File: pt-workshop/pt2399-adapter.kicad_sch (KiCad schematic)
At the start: 24 parts, among them U201 L78L05, U202 PT2399-Detailed

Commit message: 10 pin socket
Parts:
- added C216: 4.7u, Capacitor_SMD:CP_Elec_4x5.4, symbol Device:C_Polarized_Small
- added R208: 10K, Resistor_SMD:R_0603_1608Metric_Pad0.98x0.95mm_HandSolder, symbol Device:R_Small
- C201, C215: footprint Capacitor_SMD:CP_Elec_5x5.4 -> Capacitor_Tantalum_SMD:CP_EIA-3216-10_Kemet-I_Pad1.58x1.35mm_HandSolder; LCSC C380314 -> (none); Mouser 710-865080440002 -> (none)
- C203: renamed from C202; footprint Capacitor_SMD:CP_Elec_4x5.4 -> Capacitor_Tantalum_SMD:CP_EIA-3216-10_Kemet-I_Pad1.58x1.35mm_HandSolder; LCSC C264238 -> (none); Mouser 710-865080440002 -> (none)
- C205: renamed from C204; footprint Capacitor_SMD:CP_Elec_4x5.4 -> Capacitor_Tantalum_SMD:CP_EIA-3216-10_Kemet-I_Pad1.58x1.35mm_HandSolder; LCSC C380314 -> (none); Mouser 710-865080440002 -> (none)
- U202: footprint Package_DIP:DIP-16_W7.62mm -> Package_SO:SOIC-16_3.9x9.9mm_P1.27mm
- renumbered C203 to C202, C205 to C204
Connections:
- net GND: now also R208.2
- net Out: now also C216.2, R208.1; no longer C213.2, R207.1
- new net: C213.2, C216.1, R207.1
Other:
- moved on the sheet: C202, C204, C206, C207, C208, C209, C210, C211, C212, C213, C214, C215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

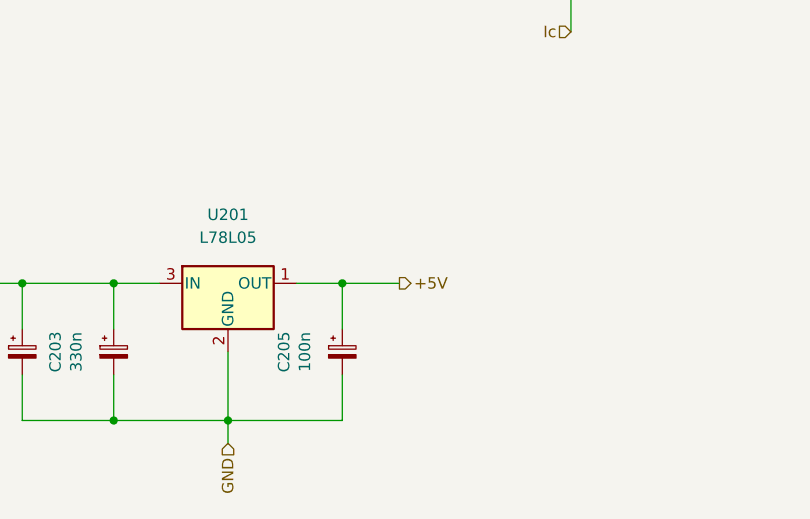
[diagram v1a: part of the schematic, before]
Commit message: Mapped components
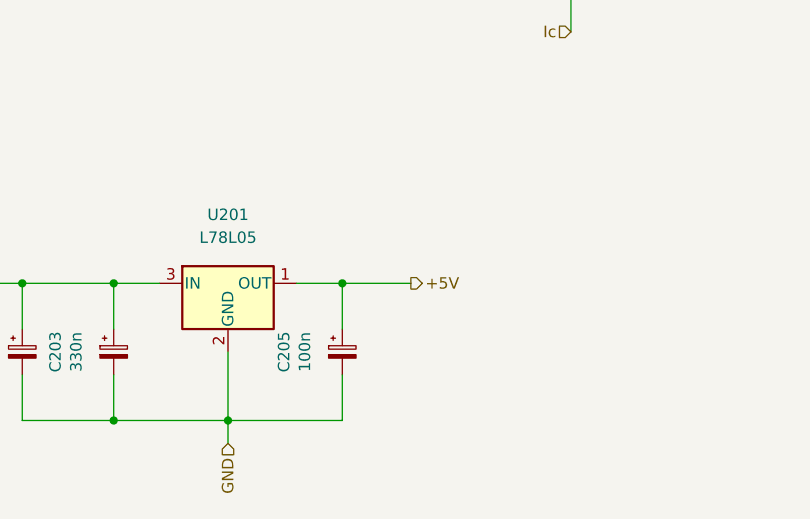
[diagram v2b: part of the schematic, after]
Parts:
- C201, C215: LCSC (none) -> C128254
- C202, C216: LCSC C213488 -> C72511
- C203: LCSC (none) -> C212667
- C205: LCSC (none) -> C1952859
- C206, C212: LCSC C107054 -> C694498
- C208, C209: LCSC C519438 -> C57112
- C210: LCSC C190576 -> C415537
- C213: LCSC C57112 -> C91367
- C214: LCSC C497032 -> C57112
- R201, R206: LCSC C100780 -> C22809
- R202, R203, R204, R205: LCSC C98220 -> C25804
- R207: LCSC C365194 -> C23189
- R208: LCSC (none) -> C25804
- U202: LCSC (none) -> C126407
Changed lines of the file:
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@@
-    (stroke (width 0) (type default) (color 0 0 0 0))
-  )
-  (wire (pts (xy 63.5 160.02) (xy 69.85 160.02))
     (stroke (width 0) (type default) (color 0 0 0 0))
   )
@@
   )
   (wire (pts (xy 180.34 83.82) (xy 180.34 91.44))
+    (stroke (width 0) (type default) (color 0 0 0 0))
+  )
+  (wire (pts (xy 63.5 160.02) (xy 71.12 160.02))
     (stroke (width 0) (type default) (color 0 0 0 0))
   )
@@
     (effects (font (size 1.27 1.27)) (justify left))
   )
-  (hierarchical_label "+5V" (shape output) (at 69.85 160.02 0)
+  (hierarchical_label "+5V" (shape output) (at 71.12 160.02 0)
     (effects (font (size 1.27 1.27)) (justify left))
   )
@@
       (effects (font (size 1.27 1.27)) hide)
     )
-    (property "LCSC" "C365194" (id 4) (at 182.88 27.94 0)
+    (property "LCSC" "C23189" (id 4) (at 182.88 27.94 0)
       (effects (font (size 1.27 1.27)) hide)
     )
@@
       (effects (font (size 1.27 1.27)) hide)
     )
-    (property "LCSC" "C107054" (id 4) (at 81.28 53.34 0)
+    (property "LCSC" "C694498" (id 4) (at 81.28 53.34 0)
       (effects (font (size 1.27 1.27)) hide)
     )
@@
       (effects (font (size 1.27 1.27)) hide)
     )
-    (property "LCSC" "C519438" (id 4) (at 134.62 132.08 0)
+    (property "LCSC" "C57112" (id 4) (at 134.62 132.08 0)
       (effects (font (size 1.27 1.27)) hide)
     )
@@
       (effects (font (size 1.27 1.27)) hide)
     )
-    (property "LCSC" "C213488" (id 4) (at 200.66 27.94 0)
+    (property "LCSC" "C72511" (id 4) (at 200.66 27.94 0)
       (effects (font (size 1.27 1.27)) hide)
     )
@@
       (effects (font (size 1.27 1.27)) hide)
     )
-    (property "LCSC" "" (id 4) (at 63.5 167.64 0)
+    (property "LCSC" "C1952859" (id 4) (at 63.5 167.64 0)
       (effects (font (size 1.27 1.27)) hide)
     )
@@
       (effects (font (size 1.27 1.27)) hide)
     )
-    (property "LCSC" "C57112" (id 4) (at 187.96 33.02 0)
+    (property "LCSC" "C91367" (id 4) (at 187.96 33.02 0)
       (effects (font (size 1.27 1.27)) hide)
     )
@@
       (effects (font (size 1.27 1.27)) hide)
     )
-    (property "LCSC" "C98220" (id 4) (at 154.94 27.94 0)
+    (property "LCSC" "C25804" (id 4) (at 154.94 27.94 0)
       (effects (font (size 1.27 1.27)) hide)
     )
@@
       (effects (font (size 1.27 1.27)) hide)
     )
-    (property "LCSC" "C100780" (id 4) (at 43.18 53.34 0)
+    (property "LCSC" "C22809" (id 4) (at 43.18 53.34 0)
       (effects (font (size 1.27 1.27)) hide)
     )
@@
       (effects (font (size 1.27 1.27)) hide)
     )
-    (property "LCSC" "C519438" (id 4) (at 139.7 129.54 0)
+    (property "LCSC" "C57112" (id 4) (at 139.7 129.54 0)
       (effects (font (size 1.27 1.27)) hide)
     )
@@
       (effects (font (size 1.27 1.27)) hide)
     )
-    (property "LCSC" "" (id 4) (at 187.96 93.98 0)
+    (property "LCSC" "C128254" (id 4) (at 187.96 93.98 0)
       (effects (font (size 1.27 1.27)) hide)
     )
@@
       (effects (font (size 1.27 1.27)) hide)
     )
-    (property "LCSC" "C100780" (id 4) (at 162.56 19.05 0)
+    (property "LCSC" "C22809" (id 4) (at 162.56 19.05 0)
       (effects (font (size 1.27 1.27)) hide)
     )
@@
       (effects (font (size 1.27 1.27)) hide)
     )
-    (property "LCSC" "C213488" (id 4) (at 30.48 53.34 0)
+    (property "LCSC" "C72511" (id 4) (at 30.48 53.34 0)
       (effects (font (size 1.27 1.27)) hide)
     )
@@
       (effects (font (size 1.27 1.27)) hide)
     )
-    (property "LCSC" "C190576" (id 4) (at 149.86 33.02 0)
+    (property "LCSC" "C415537" (id 4) (at 149.86 33.02 0)
       (effects (font (size 1.27 1.27)) hide)
     )
@@
       (effects (font (size 1.27 1.27)) hide)
     )
-    (property "LCSC" "C497032" (id 4) (at 187.96 83.82 0)
+    (property "LCSC" "C57112" (id 4) (at 187.96 83.82 0)
       (effects (font (size 1.27 1.27)) hide)
     )
@@
       (effects (font (size 1.27 1.27)) hide)
     )
-    (property "LCSC" "" (id 4) (at 27.94 167.64 0)
+    (property "LCSC" "C128254" (id 4) (at 27.94 167.64 0)
       (effects (font (size 1.27 1.27)) hide)
     )
@@
       (effects (font (size 1.27 1.27)) hide)
     )
-    (property "LCSC" "C98220" (id 4) (at 142.24 27.94 0)
+    (property "LCSC" "C25804" (id 4) (at 142.24 27.94 0)
       (effects (font (size 1.27 1.27)) hide)
     )
@@
     )
     (property "Datasheet" "https://www.electrosmash.com/pt2399-analysis" (id 3) (at 181.61 92.075 0)
+      (effects (font (size 1.27 1.27)) hide)
+    )
+    (property "LCSC" "C126407" (id 4) (at 124.46 88.9 0)
       (effects (font (size 1.27 1.27)) hide)
     )
@@
       (effects (font (size 1.27 1.27)) hide)
     )
-    (property "LCSC" "C107054" (id 4) (at 167.64 27.94 0)
+    (property "LCSC" "C694498" (id 4) (at 167.64 27.94 0)
       (effects (font (size 1.27 1.27)) hide)
     )
@@
       (effects (font (size 1.27 1.27)) hide)
     )
-    (property "LCSC" "" (id 4) (at 38.1 167.64 0)
+    (property "LCSC" "C212667" (id 4) (at 38.1 167.64 0)
       (effects (font (size 1.27 1.27)) hide)
     )
@@
       (effects (font (size 1.27 1.27)) hide)
     )
-    (property "LCSC" "C98220" (id 4) (at 66.04 53.34 0)
+    (property "LCSC" "C25804" (id 4) (at 66.04 53.34 0)
       (effects (font (size 1.27 1.27)) hide)
     )
@@
       (effects (font (size 1.27 1.27)) hide)
     )
-    (property "LCSC" "C98220" (id 4) (at 66.04 40.64 0)
+    (property "LCSC" "C25804" (id 4) (at 66.04 40.64 0)
       (effects (font (size 1.27 1.27)) hide)
     )
@@
       (effects (font (size 1.27 1.27)) hide)
     )
+    (property "LCSC" "C25804" (id 4) (at 214.63 33.02 0)
+      (effects (font (size 1.27 1.27)) hide)
+    )

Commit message: wip
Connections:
- net In: now also C202.2; no longer C202.1
- net at R201.1: now also C202.1; no longer C202.2
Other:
- moved on the sheet: C202
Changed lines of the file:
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@@
     (pin "2")
   )
-  (symbol (lib_id "Device:C_Polarized_Small") (at 30.48 53.34 90) (unit 1)
+  (symbol (lib_id "Device:C_Polarized_Small") (at 30.48 53.34 270) (mirror x) (unit 1)
     (in_bom yes) (on_board yes)
     (property "Reference" "C202" (id 0) (at 30.48 48.26 90))

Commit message: jlc
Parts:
- C208, C209, C214: LCSC C57112 -> C497032
- C213: LCSC C91367 -> C3836718
- R202, R203, R204, R205: Mouser 603-RT0603DRE1010KL -> (none)
- U201: LCSC C347258 -> C42738
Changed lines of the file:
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@@
       (effects (font (size 1.27 1.27)) hide)
     )
-    (property "LCSC" "C57112" (id 4) (at 134.62 132.08 0)
+    (property "LCSC" "C497032" (id 4) (at 134.62 132.08 0)
       (effects (font (size 1.27 1.27)) hide)
     )
@@
       (effects (font (size 1.27 1.27)) hide)
     )
-    (property "LCSC" "C91367" (id 4) (at 187.96 33.02 0)
+    (property "LCSC" "C3836718" (id 4) (at 187.96 33.02 0)
       (effects (font (size 1.27 1.27)) hide)
     )
@@
       (effects (font (size 1.27 1.27)) hide)
     )
-    (property "Mouser" "603-RT0603DRE1010KL" (id 5) (at 154.94 27.94 0)
+    (property "Mouser" "" (id 5) (at 154.94 27.94 0)
       (effects (font (size 1.27 1.27)) hide)
     )
@@
       (effects (font (size 1.27 1.27)) hide)
     )
-    (property "LCSC" "C57112" (id 4) (at 139.7 129.54 0)
+    (property "LCSC" "C497032" (id 4) (at 139.7 129.54 0)
       (effects (font (size 1.27 1.27)) hide)
     )
@@
       (effects (font (size 1.27 1.27)) hide)
     )
-    (property "LCSC" "C57112" (id 4) (at 187.96 83.82 0)
+    (property "LCSC" "C497032" (id 4) (at 187.96 83.82 0)
       (effects (font (size 1.27 1.27)) hide)
     )
@@
       (effects (font (size 1.27 1.27)) hide)
     )
-    (property "Mouser" "603-RT0603DRE1010KL" (id 5) (at 142.24 27.94 0)
+    (property "Mouser" "" (id 5) (at 142.24 27.94 0)
       (effects (font (size 1.27 1.27)) hide)
     )
@@
       (effects (font (size 1.27 1.27)) hide)
     )
-    (property "Mouser" "603-RT0603DRE1010KL" (id 5) (at 66.04 53.34 0)
+    (property "Mouser" "" (id 5) (at 66.04 53.34 0)
       (effects (font (size 1.27 1.27)) hide)
     )
@@
       (effects (font (size 1.27 1.27)) hide)
     )
-    (property "Mouser" "603-RT0603DRE1010KL" (id 5) (at 66.04 40.64 0)
+    (property "Mouser" "" (id 5) (at 66.04 40.64 0)
       (effects (font (size 1.27 1.27)) hide)
     )
@@
       (effects (font (size 1.27 1.27)) hide)
     )
-    (property "LCSC" "C347258" (id 4) (at 50.8 160.02 0)
-      (effects (font (size 1.27 1.27)) hide)
-    )
+    (property "LCSC" "C42738" (id 4) (at 50.8 160.02 0)
+      (effects (font (size 1.27 1.27)) hide)
+    )

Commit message: PTT schem export
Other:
- company: (none) -> Pedal Markt
- title: (none) -> PTT
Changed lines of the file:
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@@
 (kicad_sch (version 20211123) (generator eeschema)
   (paper "A4")
+  (title_block
+    (title "PTT")
+    (date "2024-05-11")
+    (rev "v1rev2")
+    (company "Pedal Markt")
+    (comment 1 "Andrey Salomatin")
+  )
   (junction (at 187.96 27.94) (diameter 0) (color 0 0 0 0)
   )

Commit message: wip
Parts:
- C201, C215: LCSC C128254 -> C128253
- C202, C216: LCSC C72511 -> C5246584
- C208, C209, C214: value 100n -> 1u; LCSC C497032 -> C15849; Mouser 80-C0603C104M5RAUTO -> (none)
- R207: value 5.6K -> 1k; LCSC C23189 -> C21190; Mouser 603-RT0603DRD075K6L -> (none)
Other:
- note added: "dnp"
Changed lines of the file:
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@@
     (title "PTT")
     (date "2024-05-11")
-    (rev "v1rev2")
+    (rev "v1rev3")
     (company "Pedal Markt")
     (comment 1 "Andrey Salomatin")
@@
     (stroke (width 0) (type default) (color 0 0 0 0))
   )
+  (text "dnp" (at 190.5 38.1 0)
+    (effects (font (size 1.27 1.27)) (justify left bottom))
+  )
   (label "DEMOD_OUT" (at 154.94 50.8 90)
     (effects (font (size 1 1)) (justify left bottom))
@@
     (in_bom yes) (on_board yes)
     (property "Reference" "R207" (id 0) (at 182.88 23.495 90))
-    (property "Value" "5.6K" (id 1) (at 182.88 25.4 90))
+    (property "Value" "1k" (id 1) (at 182.88 25.4 90))
     (property "Footprint" "Resistor_SMD:R_0603_1608Metric_Pad0.98x0.95mm_HandSolder" (id 2) (at 182.88 27.94 0)
       (effects (font (size 1.27 1.27)) hide)
@@
       (effects (font (size 1.27 1.27)) hide)
     )
-    (property "LCSC" "C23189" (id 4) (at 182.88 27.94 0)
-      (effects (font (size 1.27 1.27)) hide)
-    )
-    (property "Mouser" "603-RT0603DRD075K6L" (id 5) (at 182.88 27.94 0)
+    (property "LCSC" "C21190" (id 4) (at 182.88 27.94 0)
+      (effects (font (size 1.27 1.27)) hide)
+    )
+    (property "Mouser" "" (id 5) (at 182.88 27.94 0)
       (effects (font (size 1.27 1.27)) hide)
     )
@@
       (effects (font (size 1.27 1.27)) (justify right))
     )
-    (property "Value" "100n" (id 1) (at 127 130.175 0)
+    (property "Value" "1u" (id 1) (at 127 130.175 0)
       (effects (font (size 1.27 1.27)) (justify right))
     )
@@
       (effects (font (size 1.27 1.27)) hide)
     )
-    (property "LCSC" "C497032" (id 4) (at 134.62 132.08 0)
+    (property "LCSC" "C15849" (id 4) (at 134.62 132.08 0)
       (effects (font (size 1.27 1.27)) hide)
     )
@@
       (effects (font (size 1.27 1.27)) hide)
     )
-    (property "Mouser" "80-C0603C104M5RAUTO" (id 6) (at 134.62 132.08 0)
+    (property "Mouser" "" (id 6) (at 134.62 132.08 0)
       (effects (font (size 1.27 1.27)) hide)
     )
@@
       (effects (font (size 1.27 1.27)) hide)
     )
-    (property "LCSC" "C72511" (id 4) (at 200.66 27.94 0)
+    (property "LCSC" "C5246584" (id 4) (at 200.66 27.94 0)
       (effects (font (size 1.27 1.27)) hide)
     )
@@
       (effects (font (size 1.27 1.27)) (justify right))
     )
-    (property "Value" "100n" (id 1) (at 142.875 130.175 0)
+    (property "Value" "1u" (id 1) (at 142.875 130.175 0)
       (effects (font (size 1.27 1.27)) (justify right))
     )
@@
       (effects (font (size 1.27 1.27)) hide)
     )
-    (property "LCSC" "C497032" (id 4) (at 139.7 129.54 0)
+    (property "LCSC" "C15849" (id 4) (at 139.7 129.54 0)
       (effects (font (size 1.27 1.27)) hide)
     )
@@
       (effects (font (size 1.27 1.27)) hide)
     )
-    (property "Mouser" "80-C0603C104M5RAUTO" (id 6) (at 139.7 129.54 0)
+    (property "Mouser" "" (id 6) (at 139.7 129.54 0)
       (effects (font (size 1.27 1.27)) hide)
     )
@@
       (effects (font (size 1.27 1.27)) hide)
     )
-    (property "LCSC" "C128254" (id 4) (at 187.96 93.98 0)
+    (property "LCSC" "C128253" (id 4) (at 187.96 93.98 0)
       (effects (font (size 1.27 1.27)) hide)
     )
@@
       (effects (font (size 1.27 1.27)) hide)
     )
-    (property "LCSC" "C72511" (id 4) (at 30.48 53.34 0)
+    (property "LCSC" "C5246584" (id 4) (at 30.48 53.34 0)
       (effects (font (size 1.27 1.27)) hide)
     )
@@
     (in_bom yes) (on_board yes)
     (property "Reference" "C214" (id 0) (at 187.96 77.4192 90))
-    (property "Value" "100n" (id 1) (at 187.96 79.7306 90))
+    (property "Value" "1u" (id 1) (at 187.96 79.7306 90))
     (property "Footprint" "Capacitor_SMD:C_0603_1608Metric_Pad1.08x0.95mm_HandSolder" (id 2) (at 184.15 84.7852 0)
       (effects (font (size 1.27 1.27)) hide)
@@
       (effects (font (size 1.27 1.27)) hide)
     )
-    (property "LCSC" "C497032" (id 4) (at 187.96 83.82 0)
+    (property "LCSC" "C15849" (id 4) (at 187.96 83.82 0)
       (effects (font (size 1.27 1.27)) hide)
     )
@@
       (effects (font (size 1.27 1.27)) hide)
     )
-    (property "Mouser" "80-C0603C104M5RAUTO" (id 6) (at 187.96 83.82 0)
+    (property "Mouser" "" (id 6) (at 187.96 83.82 0)
       (effects (font (size 1.27 1.27)) hide)
     )
@@
       (effects (font (size 1.27 1.27)) hide)
     )
-    (property "LCSC" "C128254" (id 4) (at 27.94 167.64 0)
-      (effects (font (size 1.27 1.27)) hide)
-    )
+    (property "LCSC" "C128253" (id 4) (at 27.94 167.64 0)
+      (effects (font (size 1.27 1.27)) hide)
+    )
